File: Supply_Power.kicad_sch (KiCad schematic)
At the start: 18 parts, among them U1 R-785.0-1.0, U2 R-78C3.3-1.0

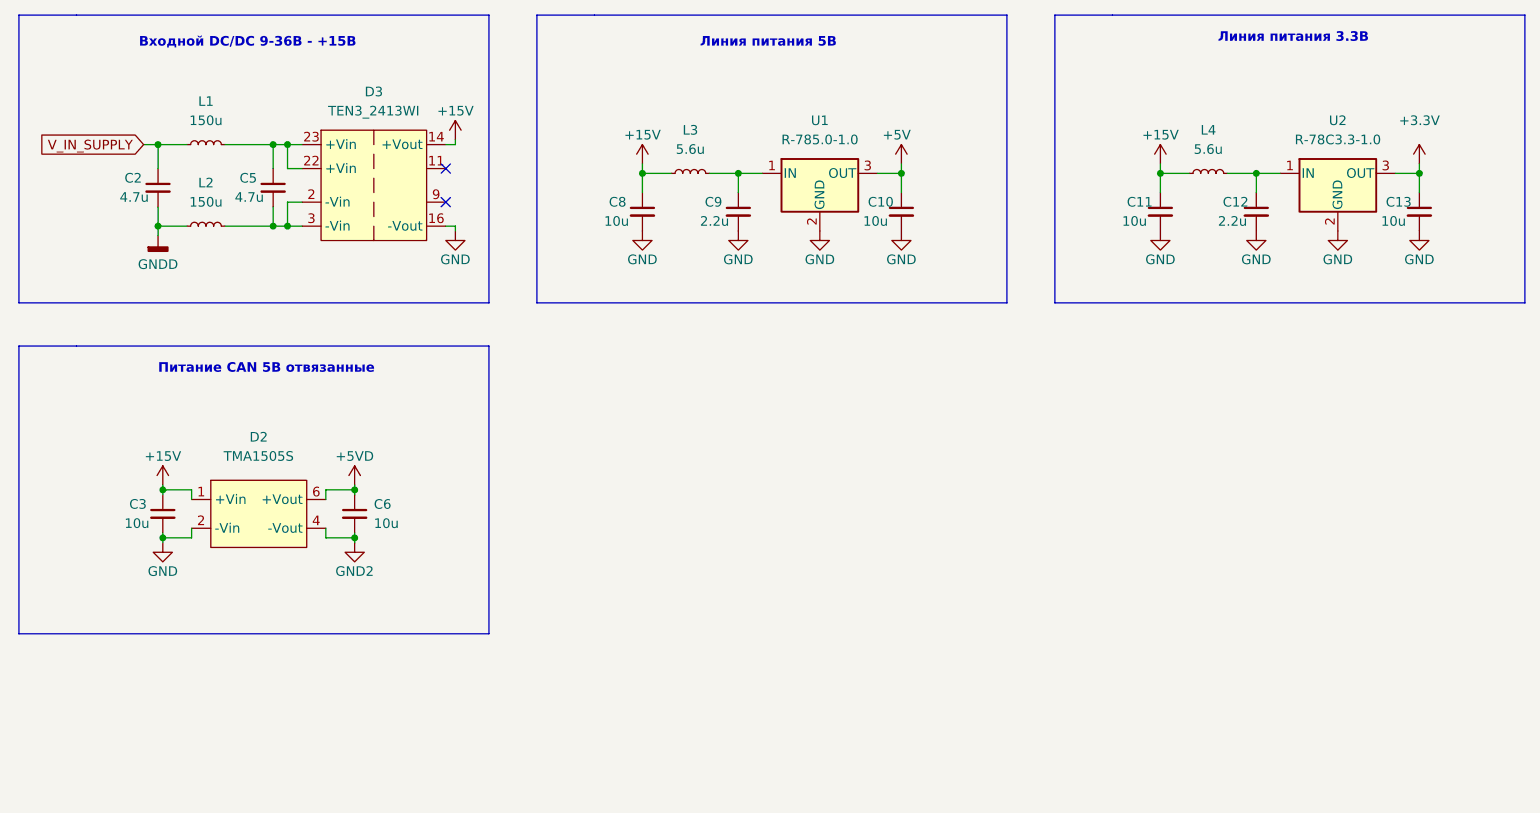
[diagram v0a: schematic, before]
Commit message: Добавил молексы и убрал питание
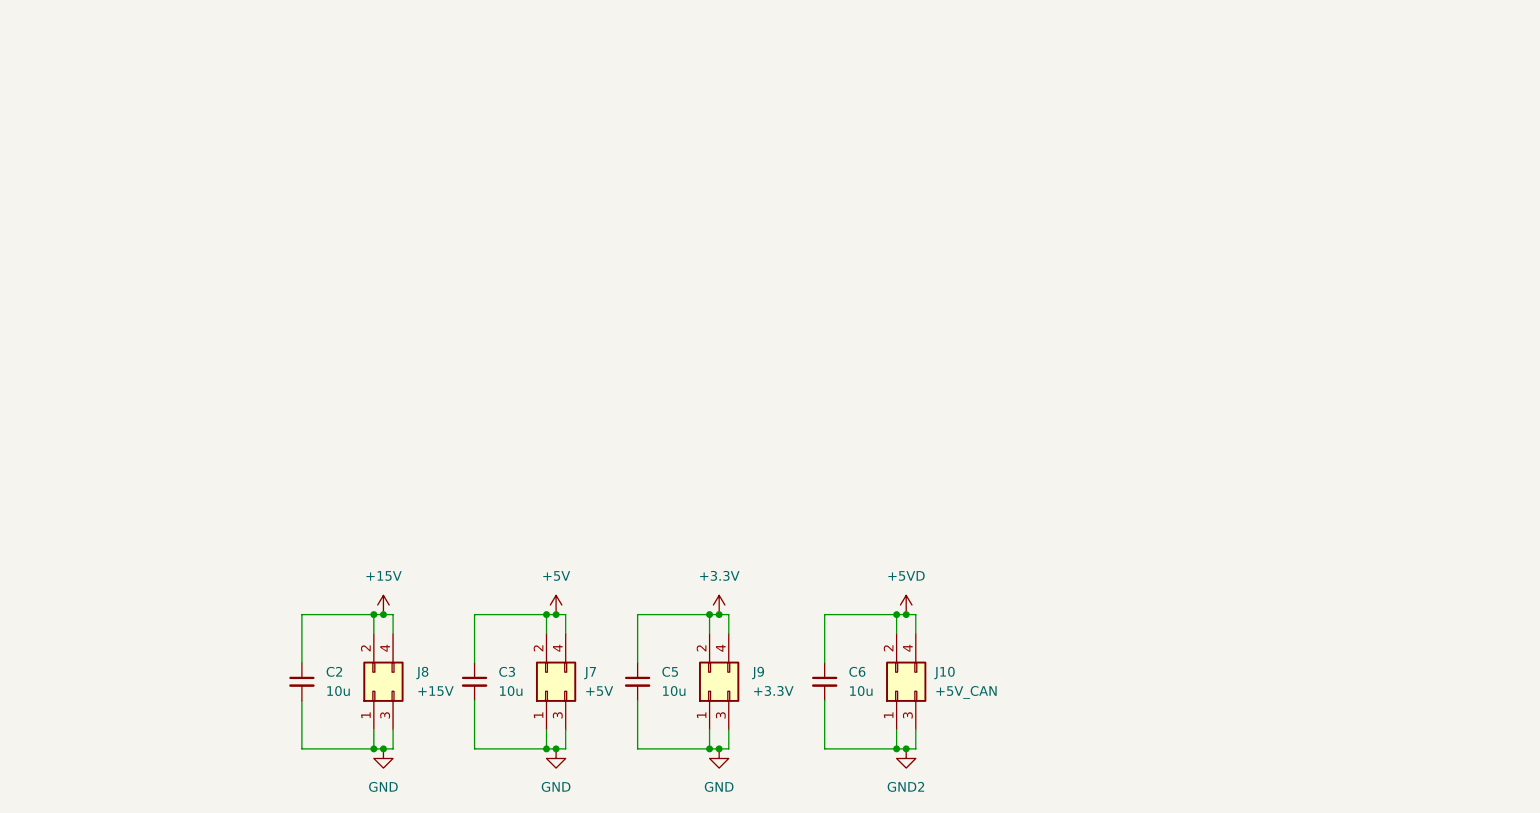
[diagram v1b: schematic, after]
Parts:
- removed C10, C11, C13, C8: 10u, Capacitor_SMD:C_1210_3225Metric_Pad1.33x2.70mm_HandSolder, symbol Device:C_Small
- removed C12, C9: 2.2u, Capacitor_SMD:C_1210_3225Metric_Pad1.33x2.70mm_HandSolder, symbol Device:C_Small
- removed D2: TMA1505S, TRACO_My:TMA1505S, symbol TRACO_My:TMA1505S
- removed D3: TEN3_2413WI, TRACO_My:TEN3_2413, symbol TRACO_My:TEN3_2413
- removed L1, L2: 150u, Inductor_SMD:L_1210_3225Metric_Pad1.42x2.65mm_HandSolder, symbol Device:L_Small
- removed L3, L4: 5.6u, Inductor_SMD:L_1210_3225Metric_Pad1.42x2.65mm_HandSolder, symbol Device:L_Small
- removed U1: R-785.0-1.0, Converter_DCDC:Converter_DCDC_RECOM_R-78E-0.5_THT, symbol Regulator_Switching:R-785.0-1.0
- removed U2: R-78C3.3-1.0, Converter_DCDC:Converter_DCDC_RECOM_R-78E-0.5_THT, symbol Regulator_Switching:R-78C3.3-1.0
- added J10: +5V_CAN, Connector_Molex:Molex_Micro-Fit_3.0_43045-0400_2x02_P3.00mm_Horizontal, symbol Connector_Generic:Conn_02x02_Odd_Even
- added J7: +5V, Connector_Molex:Molex_Micro-Fit_3.0_43045-0400_2x02_P3.00mm_Horizontal, symbol Connector_Generic:Conn_02x02_Odd_Even
- added J8: +15V, Connector_Molex:Molex_Micro-Fit_3.0_43045-0400_2x02_P3.00mm_Horizontal, symbol Connector_Generic:Conn_02x02_Odd_Even
- added J9: +3.3V, Connector_Molex:Molex_Micro-Fit_3.0_43045-0400_2x02_P3.00mm_Horizontal, symbol Connector_Generic:Conn_02x02_Odd_Even
- C2, C5: value 4.7u -> 10u
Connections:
- net GNDD is gone; now on net GND: C2.2
- net V_IN_SUPPLY is gone; now on net +15V: C2.1
- net +15V: now also J8.2 (Pin_2), J8.4 (Pin_4); no longer C3.1
- net +3V3: now also C5.1, J9.2 (Pin_2), J9.4 (Pin_4)
- net +5V: now also C3.1, J7.2 (Pin_2), J7.4 (Pin_4)
- net +5VD: now also J10.2 (Pin_2), J10.4 (Pin_4)
- net GND: now also C5.2, J7.1 (Pin_1), J7.3 (Pin_3), J8.1 (Pin_1), J8.3 (Pin_3), J9.1 (Pin_1), J9.3 (Pin_3)
- net GND2: now also J10.1 (Pin_1), J10.3 (Pin_3)
- no-connect marks 2 -> 0
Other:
- note removed: "Входной DC/DC 9-36В - +15В"
- note removed: "Линия питания 3.3В"
- note removed: "Линия питания 5В"
- note removed: "Питание CAN 5В отвязанные"
